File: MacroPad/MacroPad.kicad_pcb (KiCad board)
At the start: 2 copper layers, 27 parts, among them SW1 CherryMX, SW10 CherryMX, SW11 CherryMX, SW12 CherryMX, SW2 CherryMX, SW3 CherryMX, SW4 CherryMX, SW5 CherryMX, SW6 CherryMX, SW7 CherryMX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

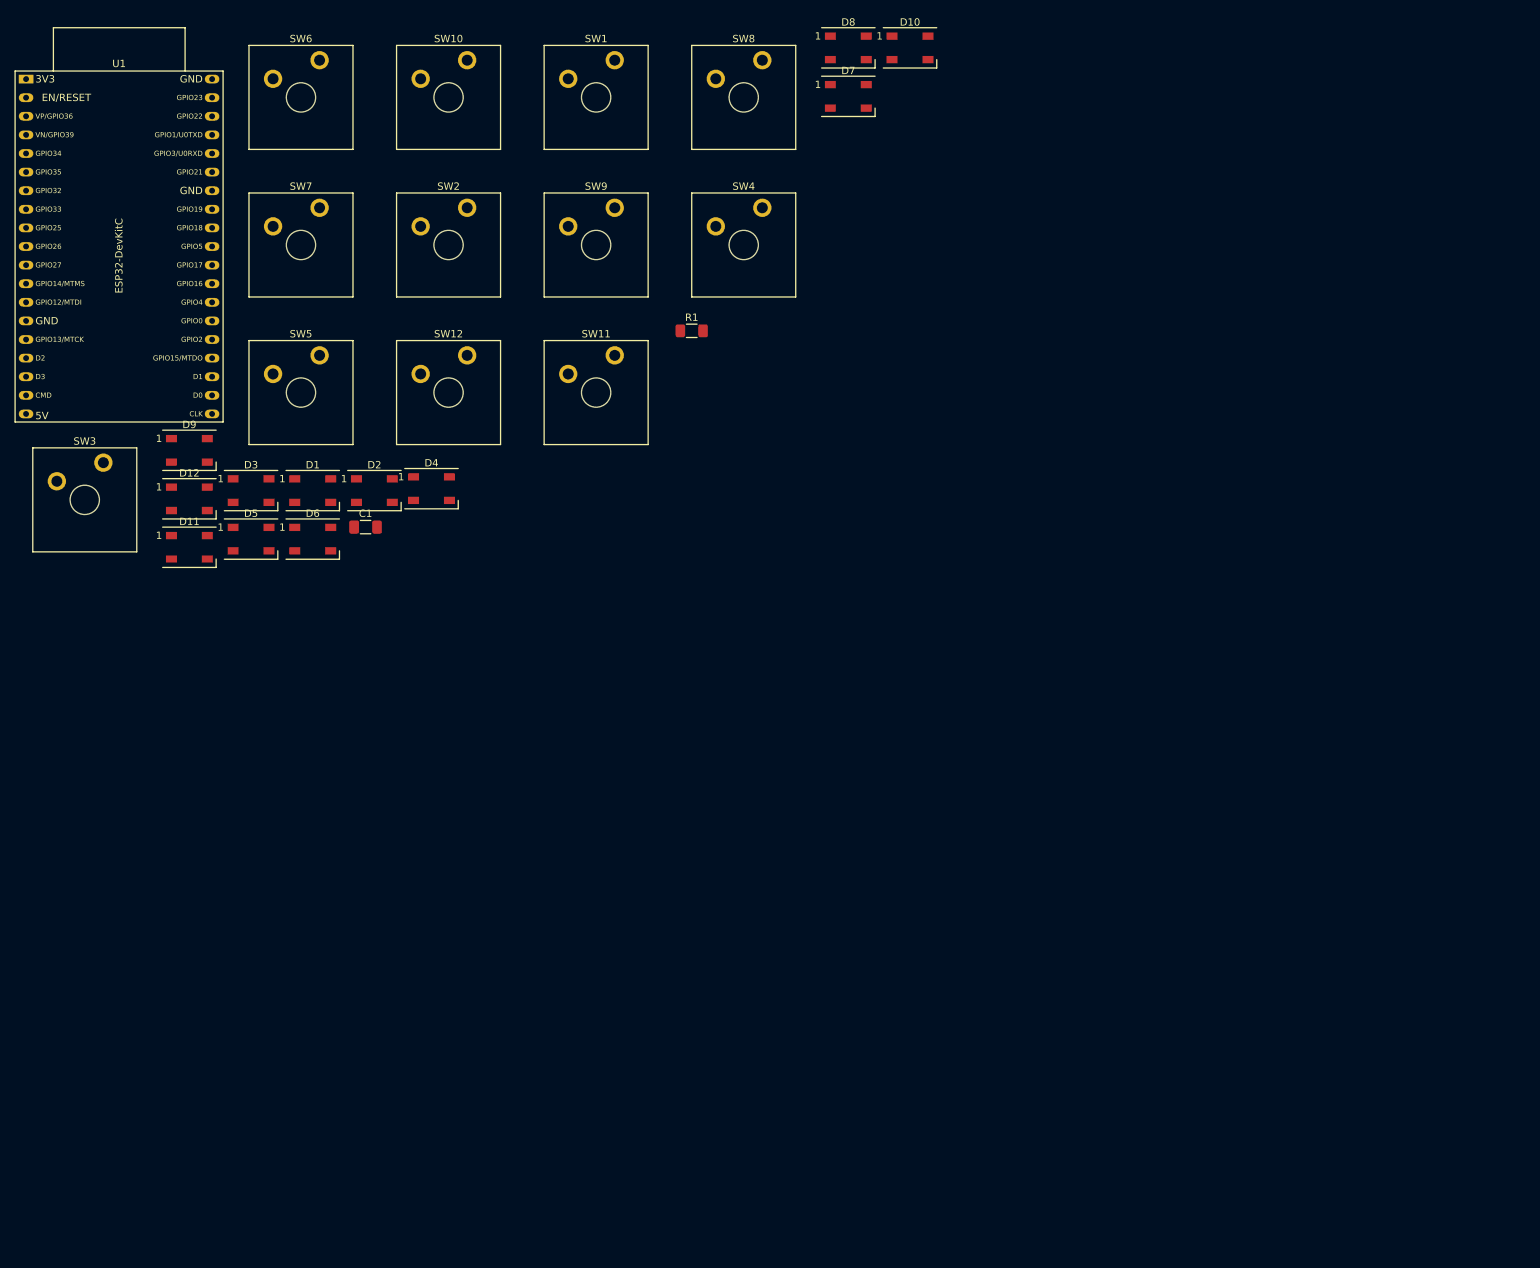
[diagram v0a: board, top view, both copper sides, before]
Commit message: Started PCB todo: ground and vin connections
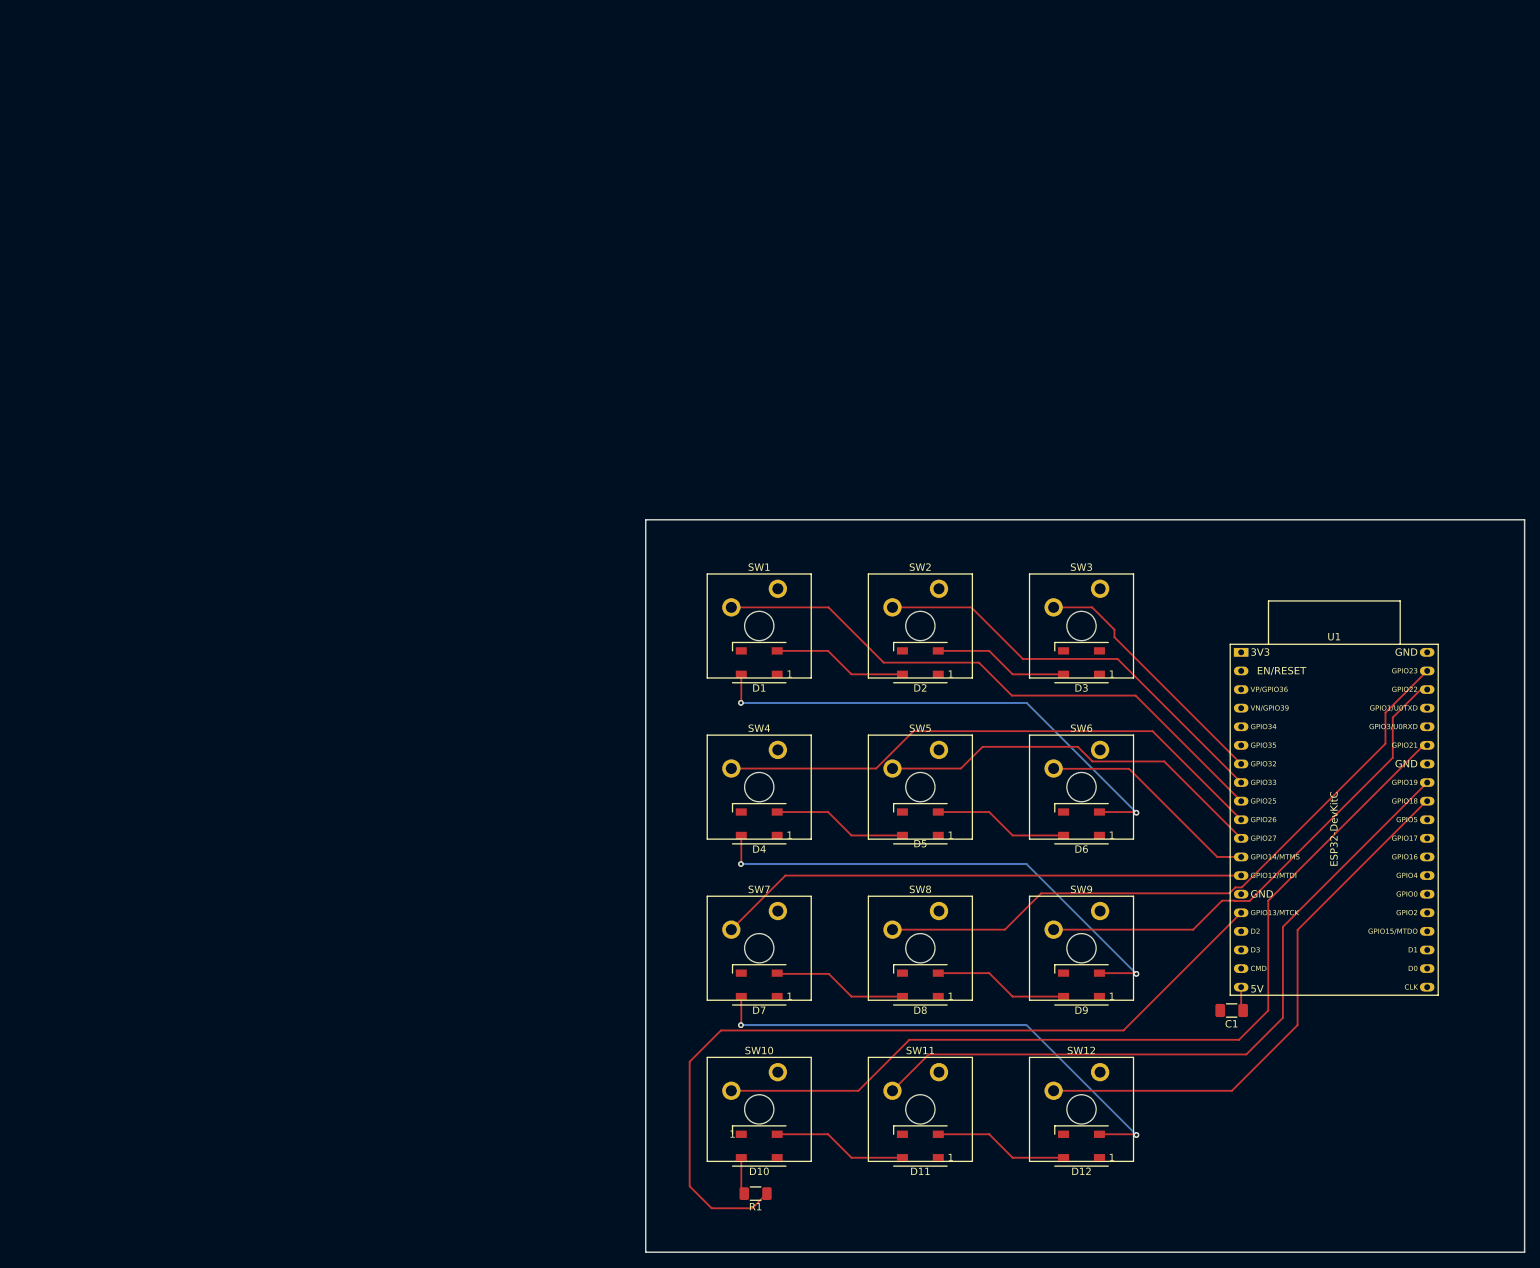
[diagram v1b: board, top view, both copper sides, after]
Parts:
- moved U1 183.4 mm to (183.3, 102.1)
- moved D10 151.3 mm to (117.5, 169.5), turned to 180 degrees
- moved D12 150.5 mm to (161.5, 169.5), turned to 180 degrees
- moved SW10 144.5 mm to (117.5, 164.5)
- moved SW6 142.2 mm to (161.5, 120.5)
- moved D9 142.0 mm to (161.5, 147.5), turned to 180 degrees
- moved SW3 137.2 mm to (161.5, 98.5)
- moved C1 135.4 mm to (182.0, 151.0), turned to 180 degrees
- moved SW12 130.6 mm to (161.5, 164.5)
- moved D11 129.0 mm to (139.5, 169.5), turned to 180 degrees
- moved D8 128.3 mm to (139.5, 147.5), turned to 180 degrees
- moved D7 121.9 mm to (117.5, 147.5), turned to 180 degrees
- moved SW8 118.6 mm to (139.5, 142.5)
- moved R1 118.1 mm to (117.0, 176.0), turned to 180 degrees
- moved SW9 116.7 mm to (161.5, 142.5)
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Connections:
- net Vin renamed Net-(C1-Pad1)
- D3 pad 2: Net-(D3-Pad2) -> unconnected-(D3-Pad2)
- D4 pad 2: unconnected-(D4-Pad2) -> Net-(D4-Pad2)
- D4 pad 4: Net-(D3-Pad2) -> Net-(D4-Pad4)
- D5 pad 4: Net-(D12-Pad2) -> Net-(D4-Pad2)
- D6 pad 2: Net-(D6-Pad2) -> Net-(D1-Pad4)
- D7 pad 4: Net-(D6-Pad2) -> Net-(D12-Pad2)
- D8 pad 2: Net-(D1-Pad4) -> Net-(D8-Pad2)
- D9 pad 2: Net-(D10-Pad4) -> Net-(D4-Pad4)
- D9 pad 4: Net-(D9-Pad4) -> Net-(D8-Pad2)
- R1 pad 2: Net-(D9-Pad4) -> Net-(D10-Pad4)
- U1 pad 7: SW1 -> SW3
- U1 pad 9: SW3 -> SW1
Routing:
- net SW10: track 0.00 -> 123.3 mm
- net DATA: track 0.00 -> 113.3 mm
- net SW11: track 0.00 -> 97.7 mm
- net SW8: track 0.00 -> 90.1 mm
- net SW1: track 0.00 -> 80.6 mm
- net SW4: track 0.00 -> 76.7 mm
- net SW12: track 0.00 -> 75.0 mm
- net SW7: track 0.00 -> 72.7 mm
- net Net-(D4-Pad4): track 0.00 -> 69.2 mm, vias 0 -> 2
- net Net-(D12-Pad2): track 0.00 -> 69.2 mm, vias 0 -> 2
- net Net-(D1-Pad4): track 0.00 -> 69.2 mm, vias 0 -> 2
- net SW9: track 0.00 -> 67.8 mm
- net SW2: track 0.00 -> 57.5 mm
- net SW5: track 0.00 -> 54.0 mm
- net SW3: track 0.00 -> 35.1 mm
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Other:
- board outline added: 120 x 100 mm

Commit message: Finished PCB i think
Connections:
- U1 pad 10: SW4 -> SW6
- U1 pad 12: SW6 -> SW4
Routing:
- net GND: track 0.00 -> 147.8 mm
- net DATA: track 113.3 -> 0.00 mm
- net SW10: track 123.3 -> 114.5 mm
- net Net-(D12-Pad2): track 69.2 -> 60.9 mm, vias 2 -> 0
- net SW12: track 75.0 -> 67.4 mm
- net Net-(D1-Pad4): track 69.2 -> 62.1 mm, vias 2 -> 0
- net Net-(D4-Pad4): track 69.2 -> 62.1 mm, vias 2 -> 0
- net SW11: track 97.7 -> 90.8 mm
- net SW5: track 54.0 -> 51.6 mm
- net SW4: track 76.7 -> 74.6 mm
- net SW6: track 30.6 -> 28.5 mm
- net SW8: track 90.1 -> 91.2 mm
- net SW3: track 35.1 -> 35.8 mm
- added copper zone on B.Cu, net GND
- added copper zone on F.Cu, net Net-(C1-Pad1)

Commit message: Updated PCB
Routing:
- net DATA: track 0.00 -> 100.0 mm
- net GND: track 147.8 -> 180.7 mm
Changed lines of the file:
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@@
   (segment (start 183.3 150.7375) (end 183.5625 151) (width 0.25) (layer "F.Cu") (net 1))
   (segment (start 183.3 147.81656) (end 183.3 150.7375) (width 0.25) (layer "F.Cu") (net 1))
-  (segment (start 159.05 167.9) (end 159.05 163.591919) (width 0.25) (layer "F.Cu") (net 2))
   (segment (start 159.05 101.9) (end 159.05 97.591919) (width 0.25) (layer "F.Cu") (net 2))
   (segment (start 137.05 123.9) (end 137.05 119.591919) (width 0.25) (layer "F.Cu") (net 2))
@@
   (segment (start 115.05 167.9) (end 115.05 163.591919) (width 0.25) (layer "F.Cu") (net 2))
   (segment (start 141.221919 159.42) (end 142.04 159.42) (width 0.25) (layer "F.Cu") (net 2))
+  (segment (start 159.05 167.9) (end 157.9 167.9) (width 0.25) (layer "F.Cu") (net 2))
   (segment (start 163.221919 93.42) (end 164.04 93.42) (width 0.25) (layer "F.Cu") (net 2))
   (segment (start 119.221919 115.42) (end 120.04 115.42) (width 0.25) (layer "F.Cu") (net 2))
-  (segment (start 160.51644 162.125479) (end 161.334521 162.125479) (width 0.25) (layer "F.Cu") (net 2))
+  (segment (start 157.9 167.9) (end 149.42 159.42) (width 0.25) (layer "F.Cu") (net 2))
+  (segment (start 172.0175 159.42) (end 164.04 159.42) (width 0.25) (layer "F.Cu") (net 2))
   (segment (start 137.05 145.9) (end 137.05 141.591919) (width 0.25) (layer "F.Cu") (net 2))
   (segment (start 141.221919 137.42) (end 142.04 137.42) (width 0.25) (layer "F.Cu") (net 2))
@@
   (segment (start 120.04 93.42) (end 119.221919 93.42) (width 0.25) (layer "F.Cu") (net 2))
   (segment (start 142.04 93.42) (end 141.221919 93.42) (width 0.25) (layer "F.Cu") (net 2))
-  (segment (start 159.05 163.591919) (end 160.51644 162.125479) (width 0.25) (layer "F.Cu") (net 2))
   (segment (start 115.05 163.591919) (end 119.221919 159.42) (width 0.25) (layer "F.Cu") (net 2))
   (segment (start 115.05 141.591919) (end 115.05 145.9) (width 0.25) (layer "F.Cu") (net 2))
   (segment (start 137.05 167.9) (end 137.05 163.591919) (width 0.25) (layer "F.Cu") (net 2))
-  (segment (start 161.334521 162.125479) (end 161.591182 161.868818) (width 0.25) (layer "F.Cu") (net 2))
   (segment (start 141.221919 115.42) (end 142.04 115.42) (width 0.25) (layer "F.Cu") (net 2))
   (segment (start 150.57 115.42) (end 142.04 115.42) (width 0.25) (layer "F.Cu") (net 2))
@@
   (segment (start 119.221919 93.42) (end 115.05 97.591919) (width 0.25) (layer "F.Cu") (net 2))
   (segment (start 137.05 141.591919) (end 141.221919 137.42) (width 0.25) (layer "F.Cu") (net 2))
+  (segment (start 180.4375 151) (end 172.0175 159.42) (width 0.25) (layer "F.Cu") (net 2))
+  (segment (start 149.42 159.42) (end 142.04 159.42) (width 0.25) (layer "F.Cu") (net 2))
   (segment (start 159.05 123.9) (end 150.57 115.42) (width 0.25) (layer "F.Cu") (net 2))
   (segment (start 159.05 145.9) (end 150.57 137.42) (width 0.25) (layer "F.Cu") (net 2))
@@
   (segment (start 150.9 167.9) (end 154.1 171.1) (width 0.25) (layer "F.Cu") (net 15))
   (segment (start 141.95 167.9) (end 150.9 167.9) (width 0.25) (layer "F.Cu") (net 15))
+  (segment (start 183.3 137.65656) (end 188 142.35656) (width 0.25) (layer "F.Cu") (net 16))
+  (segment (start 119.55 177) (end 118.55 176) (width 0.25) (layer "F.Cu") (net 16))
+  (segment (start 188 142.35656) (end 188 158) (width 0.25) (layer "F.Cu") (net 16))
+  (segment (start 169 177) (end 119.55 177) (width 0.25) (layer "F.Cu") (net 16))
+  (segment (start 188 158) (end 169 177) (width 0.25) (layer "F.Cu") (net 16))
   (segment (start 113.69 95.96) (end 120.96 95.96) (width 0.25) (layer "B.Cu") (net 17))
   (segment (start 120.96 95.96) (end 136 111) (width 0.25) (layer "B.Cu") (net 17))
